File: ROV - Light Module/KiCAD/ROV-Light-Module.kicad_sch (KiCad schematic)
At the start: 52 parts, among them J4 Bottom - Middle, J6 Main In, J7 Bottom - Middle, J8 Middle - Top, J9 Middle - Top, U1 AL8805W5, U2 ATtiny1614-Arduino, U3 AP63205WU, U6 MAX3072E

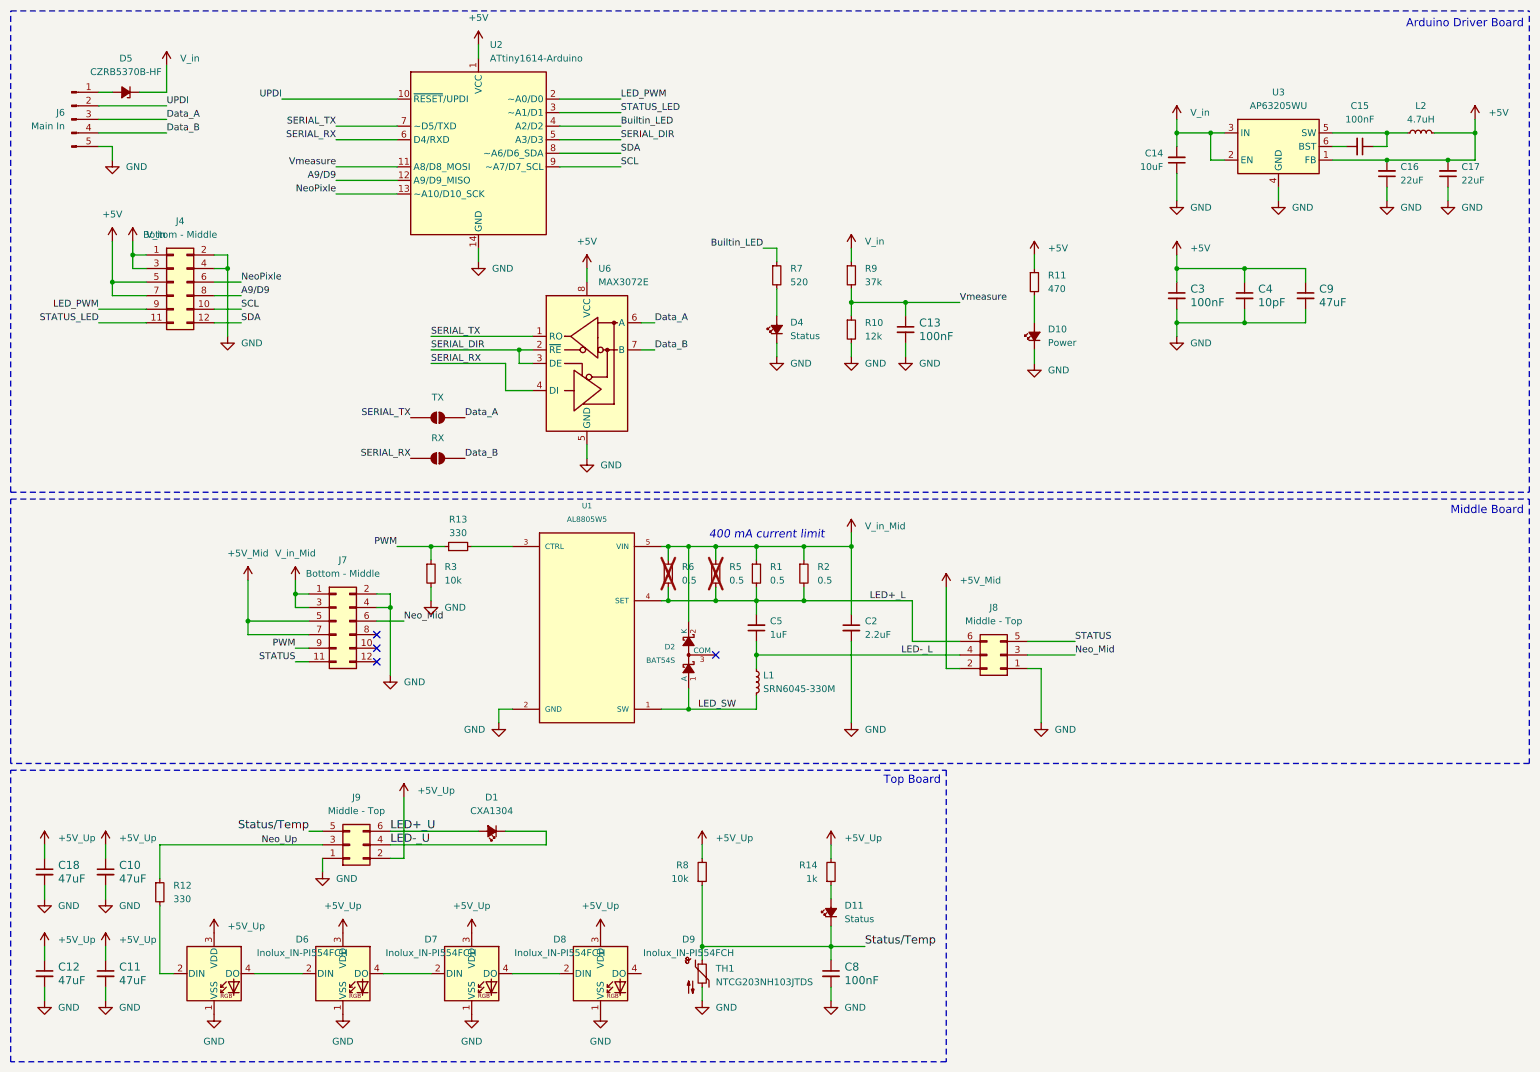
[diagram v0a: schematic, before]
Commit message: moved the arduino to seperet schematic
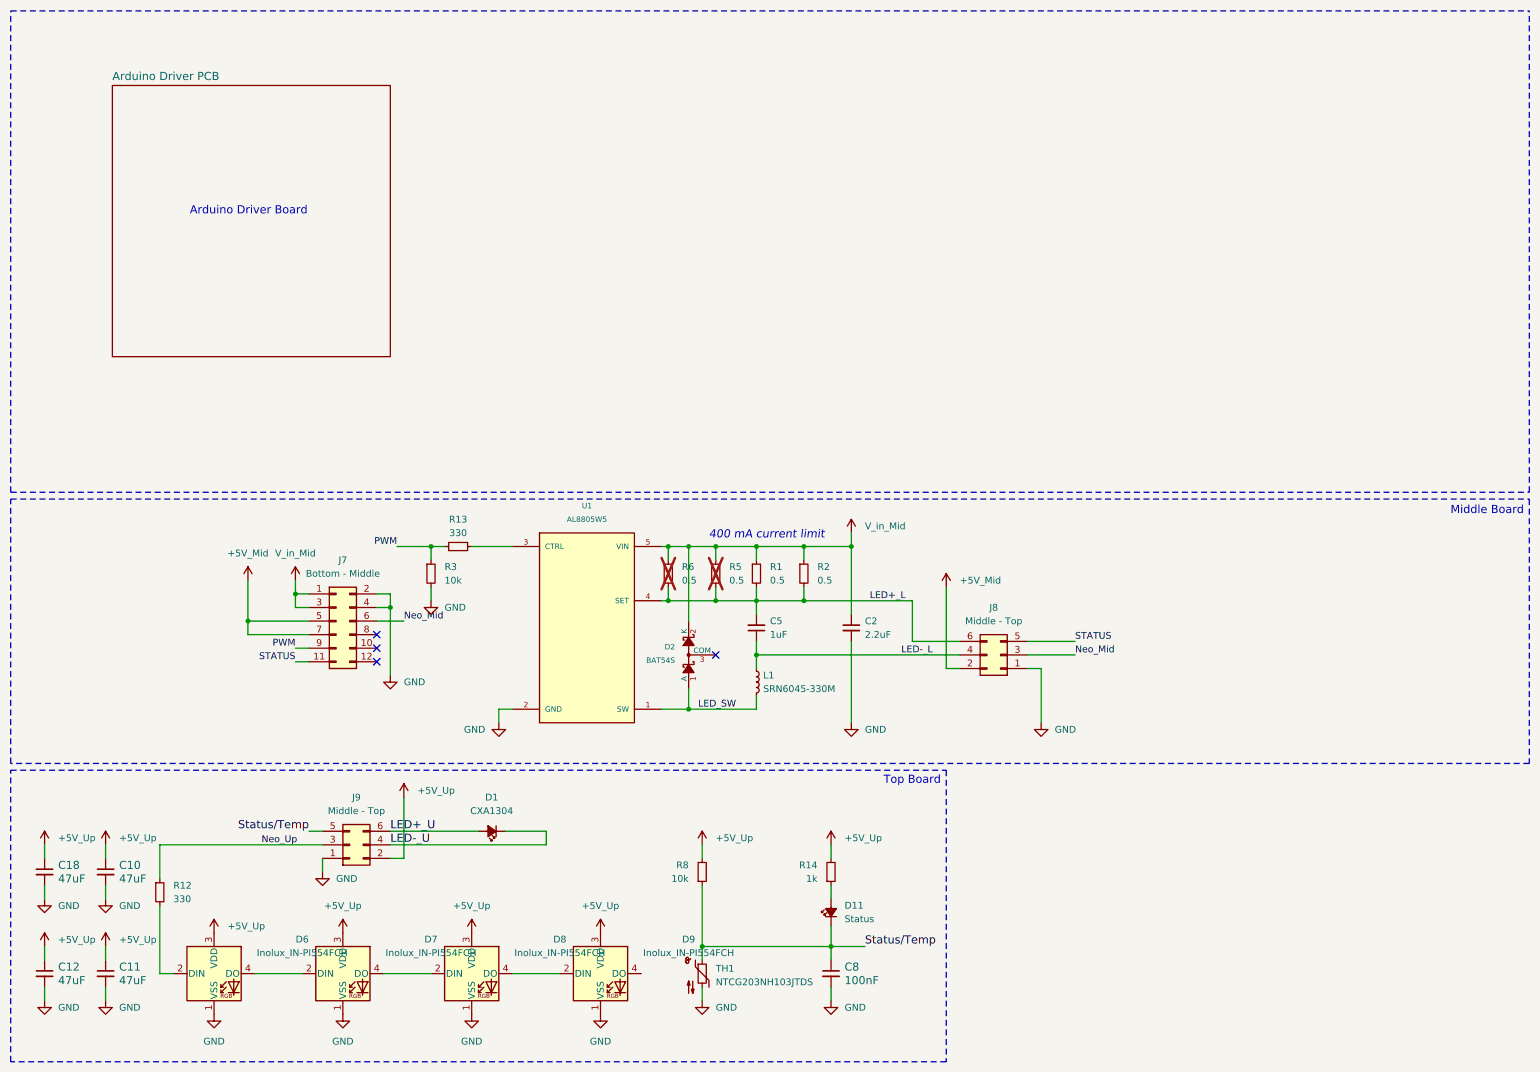
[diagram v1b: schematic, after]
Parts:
- removed C13, C15, C3: 100nF, Capacitor_SMD:C_0805_2012Metric_Pad1.18x1.45mm_HandSolder, symbol Device:C_Small
- removed C14: 10uF, Capacitor_SMD:C_0805_2012Metric_Pad1.18x1.45mm_HandSolder, symbol Device:C_Small
- removed C16, C17: 22uF, Capacitor_SMD:C_0805_2012Metric_Pad1.18x1.45mm_HandSolder, symbol Device:C_Small
- removed C4: 10pF, Capacitor_SMD:C_0805_2012Metric_Pad1.18x1.45mm_HandSolder, symbol Device:C_Small
- removed C9: 47uF, Capacitor_SMD:C_0805_2012Metric_Pad1.18x1.45mm_HandSolder, symbol Device:C_Small
- removed D10: Power, LED_SMD:LED_0805_2012Metric_Pad1.15x1.40mm_HandSolder, symbol Device:LED_Small_Filled
- removed D4: Status, LED_SMD:LED_0805_2012Metric_Pad1.15x1.40mm_HandSolder, symbol Device:LED_Small_Filled
- removed D5: CZRB5370B-HF, Diode_SMD:D_SMB_Handsoldering, symbol Partsbox:CZRB5370B-HF
- removed J4: Bottom - Middle, Connector_PinSocket_1.27mm:PinSocket_2x06_P1.27mm_Vertical_SMD, symbol Connector_Generic:Conn_02x06_Odd_Even
- removed J6: Main In, Connector_PinHeader_2.54mm:PinHeader_1x05_P2.54mm_Vertical, symbol Connector:Conn_01x05_Pin
- removed JP1: TX, Jumper:SolderJumper-2_P1.3mm_Open_TrianglePad1.0x1.5mm, symbol Jumper:SolderJumper_2_Open
- removed JP2: RX, Jumper:SolderJumper-2_P1.3mm_Open_TrianglePad1.0x1.5mm, symbol Jumper:SolderJumper_2_Open
- removed L2: 4.7uH, Inductor_SMD:L_Vishay_IHLP-1212, symbol Device:L_Small
- removed R10: 12k, Resistor_SMD:R_0805_2012Metric_Pad1.20x1.40mm_HandSolder, symbol Device:R_Small
- removed R11: 470, Resistor_SMD:R_0805_2012Metric_Pad1.20x1.40mm_HandSolder, symbol Device:R_Small
- removed R7: 520, Resistor_SMD:R_0805_2012Metric_Pad1.20x1.40mm_HandSolder, symbol Device:R_Small
- removed R9: 37k, Resistor_SMD:R_0805_2012Metric_Pad1.20x1.40mm_HandSolder, symbol Device:R_Small
- removed U2: ATtiny1614-Arduino, Package_SO:SOIC-14_3.9x8.7mm_P1.27mm, symbol KiCad Symbols:ATtiny1614-Arduino
- removed U3: AP63205WU, Package_TO_SOT_SMD:TSOT-23-6, symbol Regulator_Switching:AP63200WU
- removed U6: MAX3072E, Package_SO:SOIC-8_3.9x4.9mm_P1.27mm, symbol Interface_UART:MAX3072E
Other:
- added sheet Arduino Driver PCB (Arduino Driver PCB.kicad_sch)

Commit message: design review
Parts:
- removed D2: BAT54S, Package_TO_SOT_SMD:SOT-23, symbol KiCad Symbols:BAT54S
- removed R5, R6: 0.5, Resistor_SMD:R_1206_3216Metric_Pad1.30x1.75mm_HandSolder, symbol Device:R_Small
- added D3: ZLLS1000TA, Package_TO_SOT_SMD:SOT-23, symbol Device:D_Schottky_Small_Filled
- C2: Voltage (none) -> 25 V+
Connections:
- net LED_SW: now also D3.1 (Annode)
- net V_in_Mid: now also D3.3 (Cathode)
- no-connect marks 4 -> 3
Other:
- note added: "C5 The AL8805 datasheet states that a capacitor can be placed across the LEDs to reduce LED-current ripple, and specifically gives 1 µF as an example."

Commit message: cleanup
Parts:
- added J4: Conn_02x05_Odd_Even, Connector_PinSocket_1.27mm:PinSocket_2x05_P1.27mm_Vertical_SMD, symbol Connector_Generic:Conn_02x05_Odd_Even
- added R4: 0.5, Resistor_SMD:R_0805_2012Metric_Pad1.20x1.40mm_HandSolder, symbol Device:R_Small
- R1, R2: footprint Resistor_SMD:R_1206_3216Metric_Pad1.30x1.75mm_HandSolder -> Resistor_SMD:R_0805_2012Metric_Pad1.20x1.40mm_HandSolder; ALT RS 223-1701 -> (none); Alt Manufactute CRM1206-FX-R510ELF -> (none); DigiKey 311-0.5LWCT-ND -> (none); Manufacture RL1206FR-070R5L -> (none); Partsbox https://partsbox.com/I24gh3zxsktgpx94e4epv1nrpe6 -> (none)
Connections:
- net GND: now also J4.2 (Pin_2), J4.4 (Pin_4)
- net LED+_L: now also R4.2
- net V_in_Mid: now also R4.1
- new net +5V: J4.3 (Pin_3)
- new net A9/D9: J4.7 (Pin_7)
- new net LED_PWM: J4.6 (Pin_6)
- new net NeoPixle: J4.5 (Pin_5)
- new net SCL: J4.8 (Pin_8)
- new net SDA: J4.10 (Pin_10)
- new net STATUS_LED: J4.9 (Pin_9)
- new net V_in: J4.1 (Pin_1)
- no-connect marks 3 -> 4
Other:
- note added: "600 mA current limit"
- note removed: "400 mA current limit"
- moved on the sheet: D1, J7

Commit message: update PCBs
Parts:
- D1: notes (none) -> Cree XLamp CXA1304, 9 V class
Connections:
- no-connect marks 4 -> 5
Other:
- sheet Arduino Driver PCB ports: added A3/D3, A9/D9, SCL, SDA, ~A0/D0, ~A10/D10_SCK, ~A1/D1; removed none
- note added: "600 mA current limit 0.5 Ω / 3 ≈ 0.167 Ω"
- note removed: "600 mA current limit"
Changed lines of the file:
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@@
 		)
 	)
-	(text "600 mA current limit"
+	(text "600 mA current limit\n0.5 Ω / 3 ≈ 0.167 Ω"
 		(exclude_from_sim no)
 		(at 137.16 105.41 0)
@@
 	)
 	(no_connect
+		(at 80.01 26.67)
+	)
+	(no_connect
 		(at 60.96 125.73)
 	)
@@
 	(wire
 		(pts
+			(xy 77.47 24.13) (xy 80.01 24.13)
+		)
+		(stroke
+			(width 0)
+			(type default)
+		)
+	)
+	(wire
+		(pts
 			(xy 130.81 106.68) (xy 130.81 124.46)
 		)
@@
 	(wire
 		(pts
+			(xy 77.47 31.75) (xy 80.01 31.75)
+		)
+		(stroke
+			(width 0)
+			(type default)
+		)
+	)
+	(wire
+		(pts
 			(xy 36.83 120.65) (xy 48.26 120.65)
 		)
@@
 	(wire
 		(pts
+			(xy 77.47 29.21) (xy 80.01 29.21)
+		)
+		(stroke
+			(width 0)
+			(type default)
+		)
+	)
+	(wire
+		(pts
 			(xy 45.72 115.57) (xy 45.72 113.03)
 		)
@@
 	(wire
 		(pts
+			(xy 77.47 21.59) (xy 80.01 21.59)
+		)
+		(stroke
+			(width 0)
+			(type default)
+		)
+	)
+	(wire
+		(pts
 			(xy 12.7 189.23) (xy 12.7 191.77)
 		)
@@
 	(wire
 		(pts
+			(xy 77.47 26.67) (xy 80.01 26.67)
+		)
+		(stroke
+			(width 0)
+			(type default)
+		)
+	)
+	(wire
+		(pts
 			(xy 95.25 64.77) (xy 104.14 64.77)
 		)
@@
 	(wire
 		(pts
+			(xy 77.47 39.37) (xy 80.01 39.37)
+		)
+		(stroke
+			(width 0)
+			(type default)
+		)
+	)
+	(wire
+		(pts
 			(xy 24.13 162.56) (xy 24.13 165.1)
 		)
@@
 	(wire
 		(pts
+			(xy 77.47 36.83) (xy 80.01 36.83)
+		)
+		(stroke
+			(width 0)
+			(type default)
+		)
+	)
+	(wire
+		(pts
 			(xy 128.27 137.16) (xy 146.05 137.16)
 		)
@@
 		)
 	)
+	(label "A9{slash}D9"
+		(at 80.01 29.21 0)
+		(effects
+			(font
+				(size 1.27 1.27)
+			)
+			(justify left bottom)
+		)
+	)
 	(label "LED_PWM"
 		(at 121.92 59.69 0)
@@
 		)
 	)
+	(label "SCL"
+		(at 80.01 36.83 0)
+		(effects
+			(font
+				(size 1.27 1.27)
+			)
+			(justify left bottom)
+		)
+	)
+	(label "LED_PWM"
+		(at 80.01 21.59 0)
+		(effects
+			(font
+				(size 1.27 1.27)
+			)
+			(justify left bottom)
+		)
+	)
 	(label "Neo_Mid"
 		(at 73.66 120.65 180)
@@
 		)
 	)
+	(label "STATUS_LED"
+		(at 80.01 24.13 0)
+		(effects
+			(font
+				(size 1.27 1.27)
+			)
+			(justify left bottom)
+		)
+	)
 	(label "LED+_L"
 		(at 173.99 116.84 180)
@@
 		)
 	)
+	(label "SDA"
+		(at 80.01 39.37 0)
+		(effects
+			(font
+				(size 1.27 1.27)
+			)
+			(justify left bottom)
+		)
+	)
 	(label "A9{slash}D9"
 		(at 95.25 62.23 180)
@@
 		)
 	)
+	(label "NeoPixle"
+		(at 80.01 31.75 0)
+		(effects
+			(font
+				(size 1.27 1.27)
+			)
+			(justify left bottom)
+		)
+	)
 	(label "Neo_Up"
 		(at 53.34 162.56 0)
@@
 		(fields_autoplaced yes)
 		(property "Reference" "D1"
-			(at 101.5365 153.67 0)
+			(at 101.5365 151.13 0)
 			(show_name no)
 			(do_not_autoplace no)
@@
 		)
 		(property "Value" "CXA1304"
-			(at 101.5365 156.21 0)
+			(at 101.5365 153.67 0)
 			(show_name no)
 			(do_not_autoplace no)
@@
 			)
 		)
+		(property "notes" "Cree XLamp CXA1304, 9 V class"
+			(at 101.5365 156.21 0)
+			(show_name no)
+			(do_not_autoplace no)
+			(effects
+				(font
+					(size 1.524 1.524)
+				)
+			)
+		)
 		(pin "1"
 		)
@@
 			)
 		)
+		(pin "A9{slash}D9" bidirectional
+			(at 77.47 29.21 0)
+			(effects
+				(font
+					(size 1.524 1.524)
+				)
+				(justify right)
+			)
+		)
+		(pin "SCL" bidirectional
+			(at 77.47 36.83 0)
+			(effects
+				(font
+					(size 1.524 1.524)
+				)
+				(justify right)
+			)
+		)
+		(pin "SDA" bidirectional
+			(at 77.47 39.37 0)
+			(effects
+				(font
+					(size 1.524 1.524)
+				)
+				(justify right)
+			)
+		)
+		(pin "~A0{slash}D0" bidirectional
+			(at 77.47 21.59 0)
+			(effects
+				(font
+					(size 1.524 1.524)
+				)
+				(justify right)
+			)
+		)
+		(pin "~A1{slash}D1" bidirectional
+			(at 77.47 24.13 0)
+			(effects
+				(font
+					(size 1.524 1.524)
+				)
+				(justify right)
+			)
+		)
+		(pin "~A10{slash}D10_SCK" bidirectional
+			(at 77.47 31.75 0)
+			(effects
+				(font
+					(size 1.524 1.524)
+				)
+				(justify right)
+			)
+		)
+		(pin "A3{slash}D3" bidirectional
+			(at 77.47 26.67 0)
+			(effects
+				(font
+					(size 1.524 1.524)
+				)
+				(justify right)
+			)
+		)
